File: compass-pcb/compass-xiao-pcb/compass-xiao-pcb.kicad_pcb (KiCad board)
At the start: 2 copper layers, 23 parts

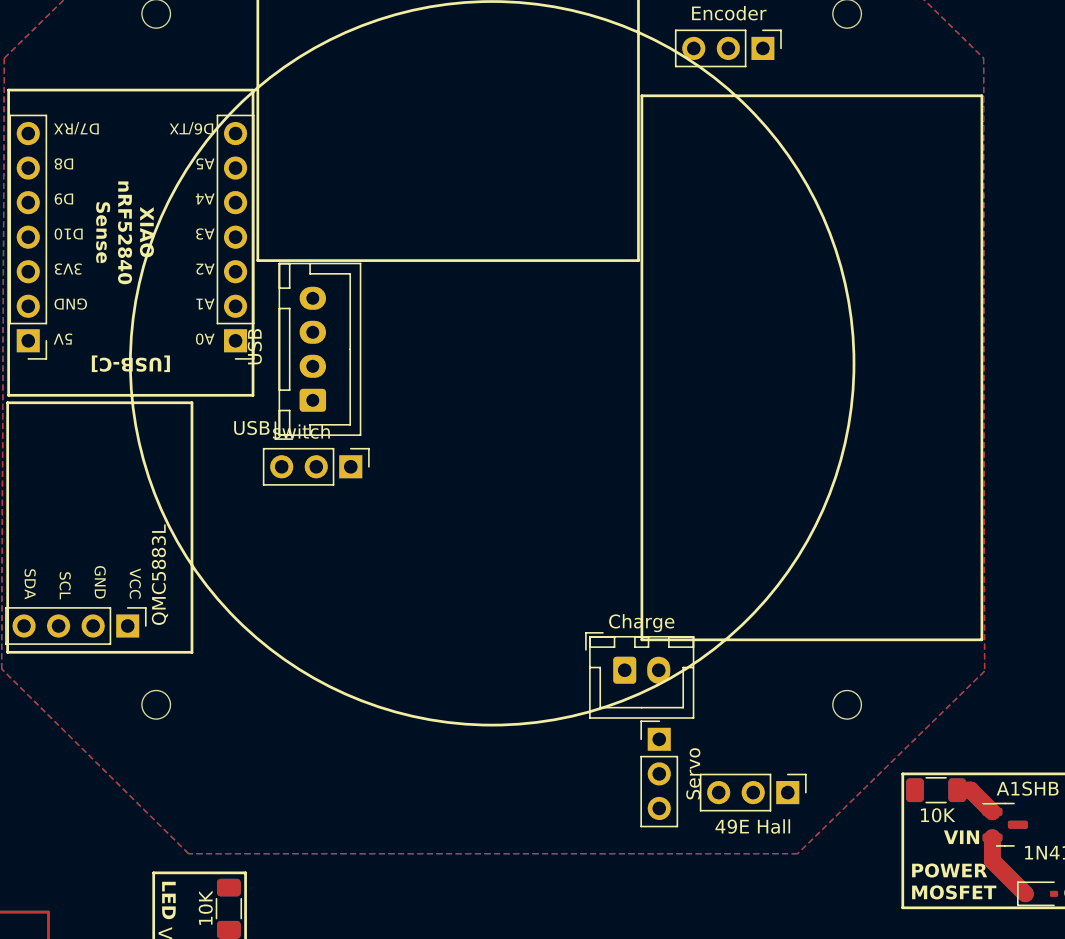
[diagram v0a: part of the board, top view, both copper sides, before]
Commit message: xiao pcb - all components, no wires
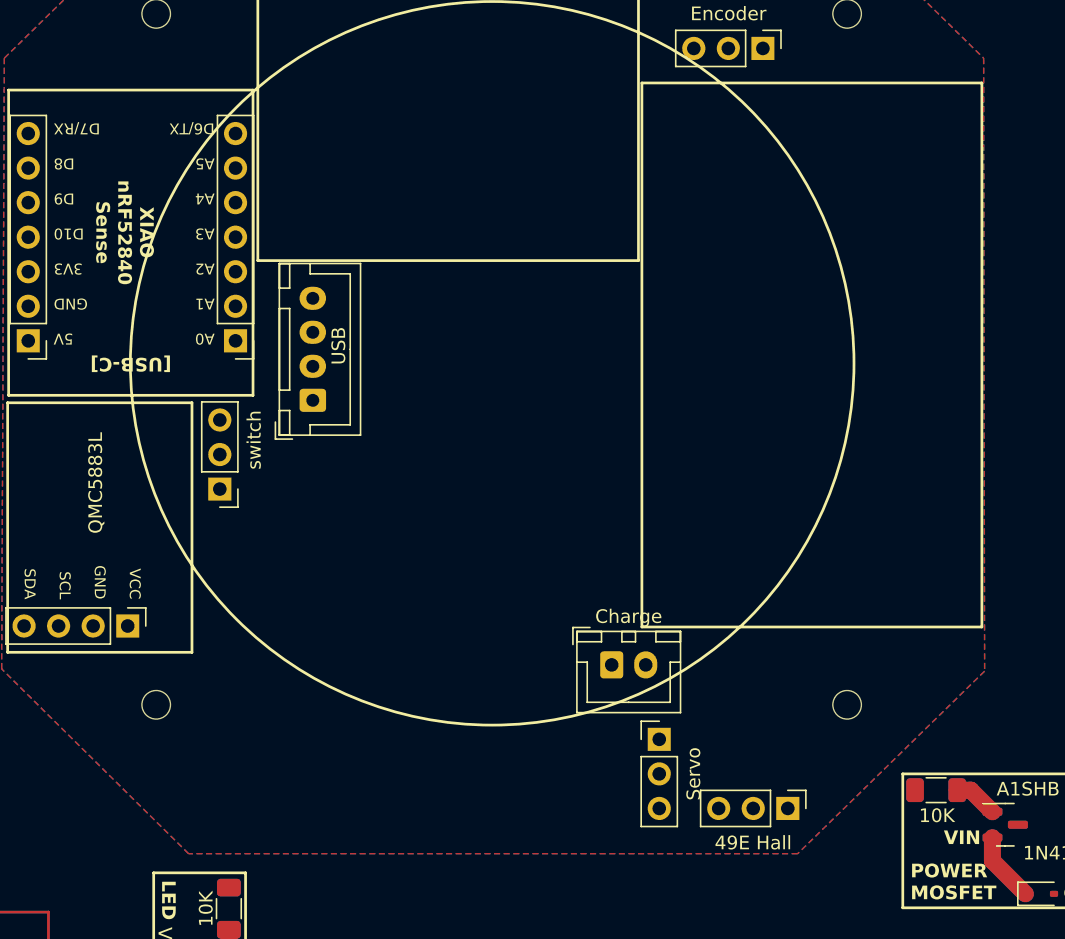
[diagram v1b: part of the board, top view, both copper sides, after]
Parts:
- moved switch 9.77 mm to (117.6, 95.9), turned to 180 degrees
- moved 49E Hall 1.16 mm to (159.3, 119.4)
- moved Charge 1.03 mm to (146.4, 108.8)
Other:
- board text removed: "USB"
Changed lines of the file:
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@@
     (tags "connector JST XH vertical")
     (attr through_hole)
-    (fp_text reference "USB" (at 3.929414 -4.225071 90) (layer "F.SilkS")
+    (fp_text reference "USB" (at 4.001155 1.911127 90) (layer "F.SilkS")
         (effects (font (size 1 1) (thickness 0.15)))
     )
@@
   )
   (footprint "Connector_JST:JST_XH_B2B-XH-A_1x02_P2.50mm_Vertical" (layer "F.Cu")
-    (at 147.32 109.22)
+    (at 146.363784 108.826184)
     (descr "JST XH series connector, B2B-XH-A (http://www.jst-mfg.com/product/pdf/eng/eXH.pdf), generated with kicad-footprint-generator")
     (tags "connector JST XH vertical")
@@
     (tags "Through hole pin header THT 1x04 2.54mm single row")
     (attr through_hole)
-    (fp_text reference "QMC5883L" (at 0 -2.33 90) (layer "F.SilkS")
+    (fp_text reference "QMC5883L" (at -6.775469 2.354575 90) (layer "F.SilkS")
         (effects (font (size 1 1) (thickness 0.15)) (justify left))
     )
@@
   )
   (footprint "Connector_PinHeader_2.54mm:PinHeader_1x03_P2.54mm_Vertical" (layer "F.Cu")
-    (at 159.308892 118.215794 -90)
+    (at 159.308892 119.38 -90)
     (descr "Through hole straight pin header, 1x03, 2.54mm pitch, single row")
     (tags "Through hole pin header THT 1x03 2.54mm single row")
@@
   )
   (footprint "Connector_PinHeader_2.54mm:PinHeader_1x03_P2.54mm_Vertical" (layer "F.Cu")
-    (at 127.180929 94.261785 -90)
+    (at 117.550317 95.899613 180)
     (descr "Through hole straight pin header, 1x03, 2.54mm pitch, single row")
     (tags "Through hole pin header THT 1x03 2.54mm single row")
     (attr through_hole)
-    (fp_text reference "switch" (at -2.54 3.611298) (layer "F.SilkS")
-        (effects (font (size 1 1) (thickness 0.15)))
-    )
-    (fp_text value "PinHeader_1x03_P2.54mm_Vertical" (at 0 7.41 90) (layer "F.Fab")
-        (effects (font (size 1 1) (thickness 0.15)))
-    )
-    (fp_text user "${REFERENCE}" (at 0 2.54) (layer "F.Fab")
+    (fp_text reference "switch" (at -2.54 3.611298 90) (layer "F.SilkS")
+        (effects (font (size 1 1) (thickness 0.15)))
+    )
+    (fp_text value "PinHeader_1x03_P2.54mm_Vertical" (at 0 7.41) (layer "F.Fab")
+        (effects (font (size 1 1) (thickness 0.15)))
+    )
+    (fp_text user "${REFERENCE}" (at 0 2.54 90) (layer "F.Fab")
         (effects (font (size 1 1) (thickness 0.15)))
     )
@@
     (fp_line (start 1.27 6.35) (end -1.27 6.35)
       (stroke (width 0.1) (type solid)) (layer "F.Fab"))
-    (pad "1" thru_hole rect (at 0 0 270) (size 1.7 1.7) (drill 1) (layers "*.Cu" "*.Mask"))
-    (pad "2" thru_hole oval (at 0 2.54 270) (size 1.7 1.7) (drill 1) (layers "*.Cu" "*.Mask"))
-    (pad "3" thru_hole oval (at 0 5.08 270) (size 1.7 1.7) (drill 1) (layers "*.Cu" "*.Mask"))
+    (pad "1" thru_hole rect (at 0 0 180) (size 1.7 1.7) (drill 1) (layers "*.Cu" "*.Mask"))
+    (pad "2" thru_hole oval (at 0 2.54 180) (size 1.7 1.7) (drill 1) (layers "*.Cu" "*.Mask"))
+    (pad "3" thru_hole oval (at 0 5.08 180) (size 1.7 1.7) (drill 1) (layers "*.Cu" "*.Mask"))
     (model "${KICAD6_3DMODEL_DIR}/Connector_PinHeader_2.54mm.3dshapes/PinHeader_1x03_P2.54mm_Vertical.wrl"
       (offset (xyz 0 0 0))
@@
   (gr_rect (start 167.76391 116.84) (end 182.88 126.686976)
     (stroke (width 0.2) (type default)) (fill none) (layer "F.SilkS"))
-  (gr_rect (start 148.582606 66.983996) (end 173.582606 106.983996)
+  (gr_rect (start 148.582606 66.04) (end 173.582606 106.04)
     (stroke (width 0.2) (type default)) (fill none) (layer "F.SilkS"))
   (gr_rect (start 201.6023 59.51285) (end 217.272647 77.620807)
@@
     (effects (font (size 0.8 0.8) (thickness 0.15)) (justify right bottom))
   )
-  (gr_text "USB" (at 119.892749 91.441934) (layer "F.SilkS")
-    (effects (font (size 1 1) (thickness 0.15)))
-  )
   (gr_text "XIAO\nnRF52840\nSense" (at 108.349333 77.033226 -90) (layer "F.SilkS")

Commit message: First iteration of wiring
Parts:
- added Bat: PinHeader_1x02_P2.54mm_Vertical, Connector_PinHeader_2.54mm:PinHeader_1x02_P2.54mm_Vertical, F.Cu at (109.1, 93.4)
- added Bat: PinHeader_1x02_P2.54mm_Vertical, Connector_PinHeader_2.54mm:PinHeader_1x02_P2.54mm_Vertical, F.Cu at (148.8, 114.9)
- REF**: value SDA, SCA, VCC -> SCL, SDA, VCC
- REF**: value RX, TX, GND -> TX, RX, GND
- moved 10K 14.4 mm to (117.9, 112.4)
- moved A1SHB 14.4 mm to (115.4, 117.4)
- moved Servo 8.55 mm to (156.6, 109.0)
- moved switch 5.30 mm to (117.9, 90.6), turned to 0 degrees
- moved REF** 3.05 mm to (154.4, 63.2), turned to 90 degrees
- moved USB 0.73 mm to (124.5, 90.1)
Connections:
- 49E Hall pad 2: (no net) -> GND
- REF** pad 2: (no net) -> GND
- REF** pad 1: (no net) -> GND
- Servo pad 1: (no net) -> GND
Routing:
- net (no net): track 11.6 -> 969.0 mm
- net GND: track 0.00 -> 6.07 mm
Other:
- board text added: "Check if we can ground one end of the battery, this will help us remove the ground battery line across the board. Will have to ground Battery minus from the XIAO too.."

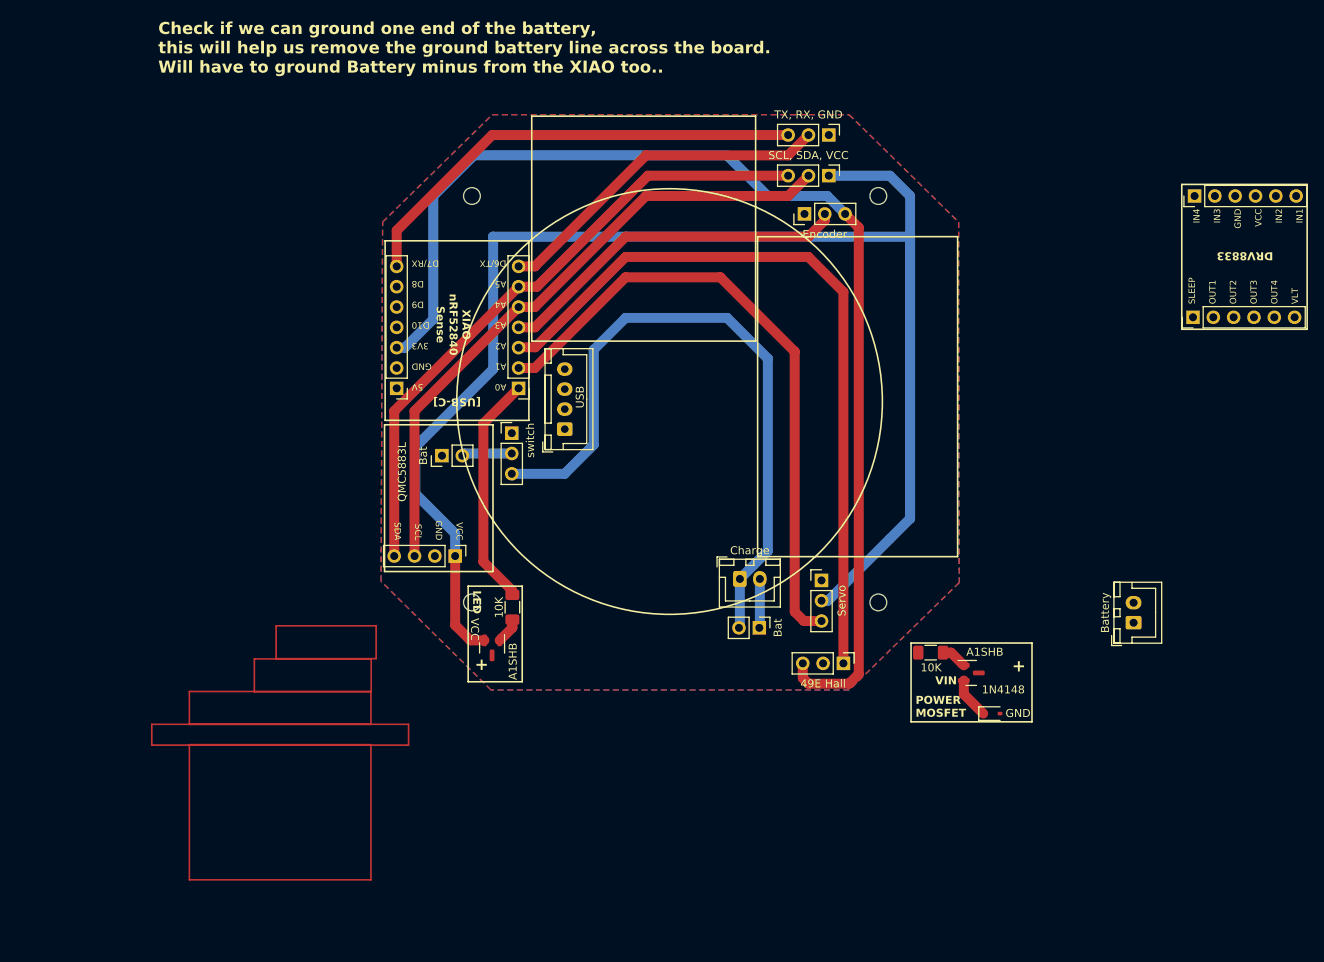
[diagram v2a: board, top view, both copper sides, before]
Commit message: added main power mosfet
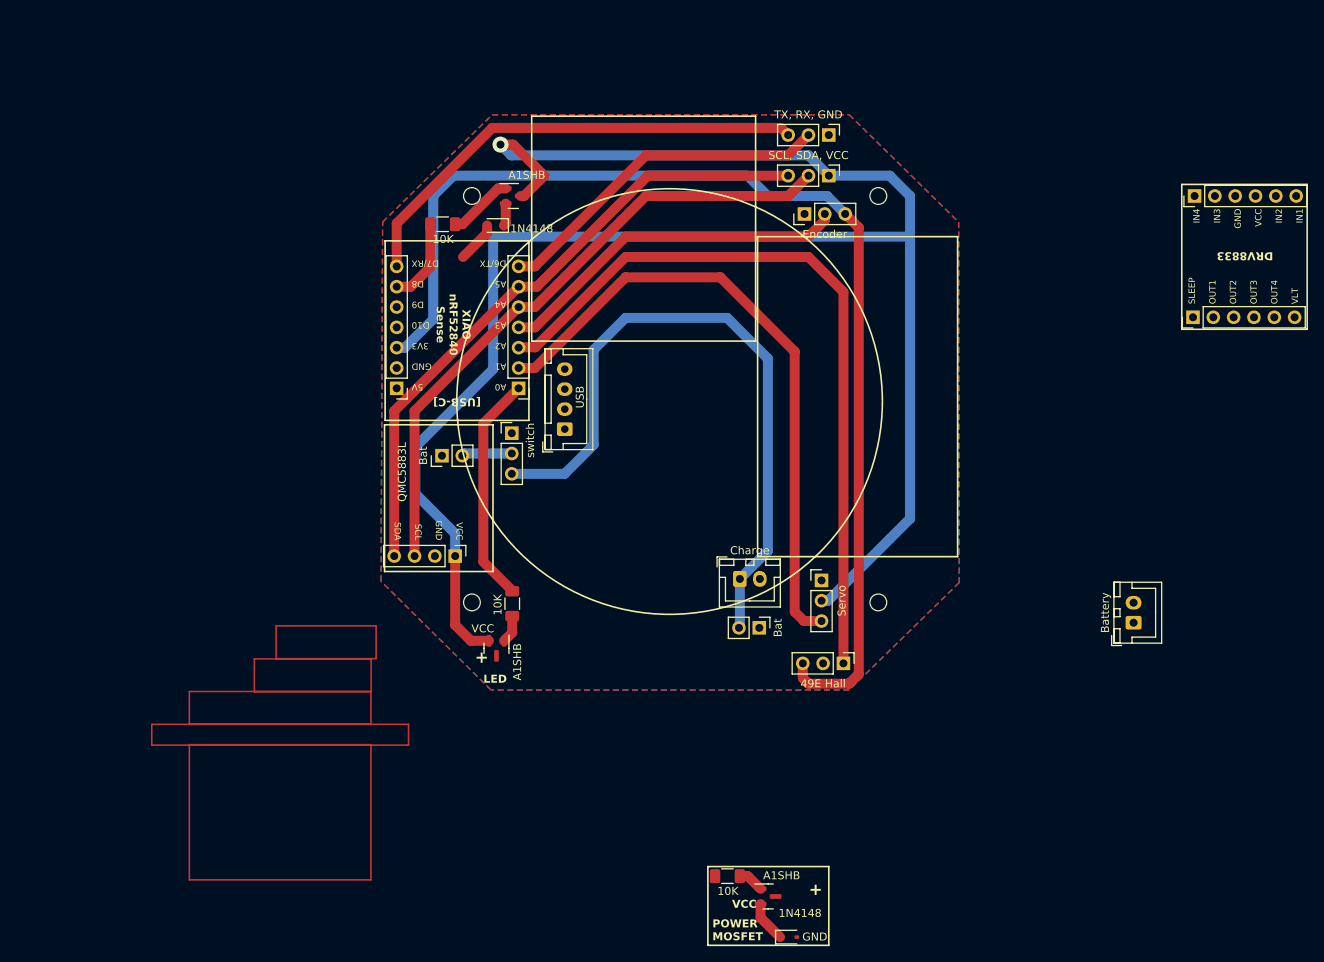
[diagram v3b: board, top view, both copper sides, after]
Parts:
- added 10K: R1002, Resistor_SMD:R_1206_3216Metric_Pad1.30x1.75mm_HandSolder, F.Cu at (109.2, 64.5)
- added 1N4148: D_SOD-323, Diode_SMD:D_SOD-323, F.Cu at (115.8, 64.6)
- added A1SHB: SOT-23, Package_TO_SOT_SMD:SOT-23, F.Cu at (118.0, 61.0)
- moved 10K 37.8 mm to (144.8, 146.0)
- moved A1SHB 37.8 mm to (149.9, 148.5)
- moved 1N4148 37.8 mm to (152.4, 153.6)
- moved A1SHB 0.55 mm to (115.9, 117.5)
- moved 10K 0.44 mm to (117.9, 111.9)
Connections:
- Charge pad 2: (no net) -> GND
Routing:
- net (no net): track 969.0 -> 1043.8 mm, vias 0 -> 1
- net GND: track 6.07 -> 5.29 mm
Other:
- board text removed: "Check if we can ground one end of the battery, this will help us remove the ground battery line across the board. Will have to ground Battery minus from the XIAO too.."
- board text removed: "VIN"

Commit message: Fixing main power line
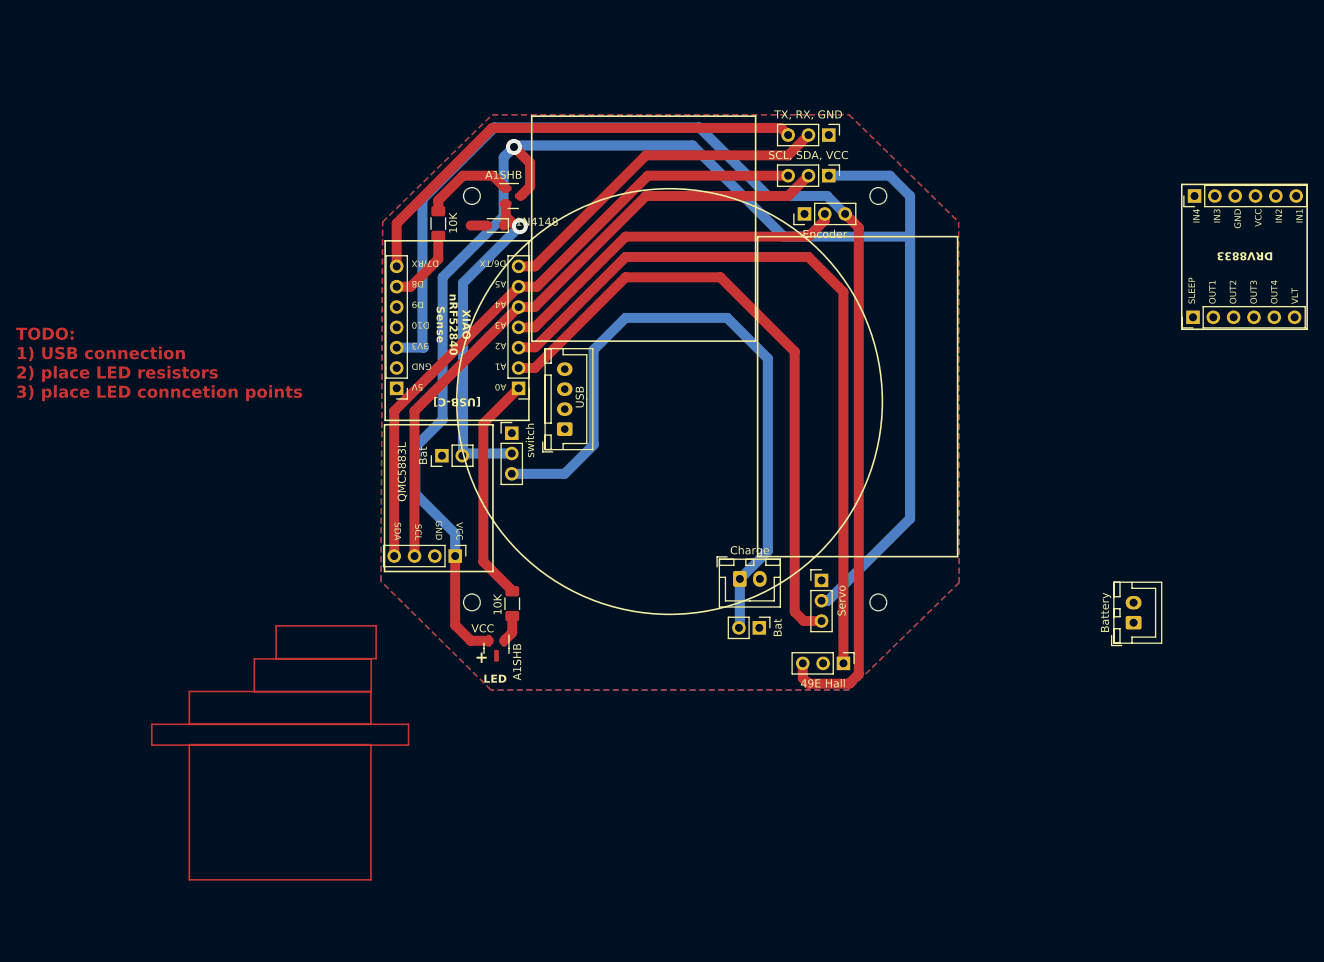
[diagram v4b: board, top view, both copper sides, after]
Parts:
- removed the 10K at (144.8, 146.0)
- removed the 1N4148 at (152.4, 153.6)
- removed the A1SHB at (149.9, 148.5)
- moved 10K 0.56 mm to (108.7, 64.4), turned to 90 degrees
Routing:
- net (no net): track 1043.8 -> 1047.1 mm, vias 1 -> 2
- net GND: track 5.29 -> 2.18 mm
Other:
- board text added: "TODO: 1) USB connection 2) place LED resistors 3) place LED conncetion points"
- board text removed: "GND"
- board text removed: "POWER MOSFET"

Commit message: minor improvements
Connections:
- Bat pad 1: (no net) -> GND
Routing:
- net (no net): track 1047.1 -> 1052.1 mm
